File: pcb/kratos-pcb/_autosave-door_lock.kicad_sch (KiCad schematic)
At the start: 8 parts, among them IC1 SN74HC595N, Q2 2N2222A, Q3 2N2222A, U2 74HC595

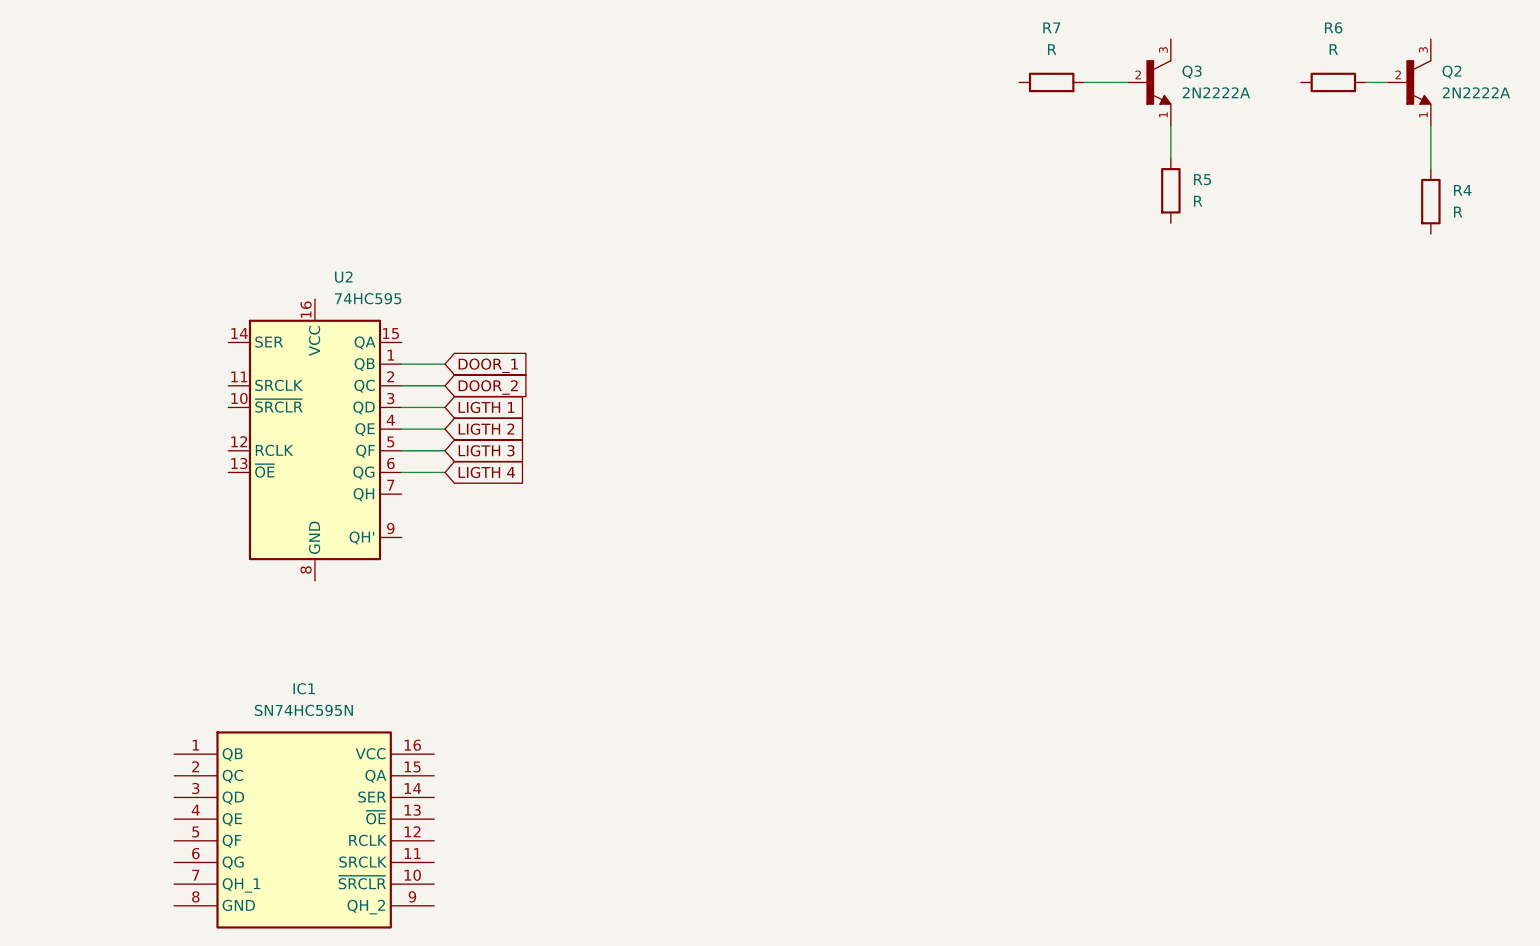
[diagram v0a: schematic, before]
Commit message: ### added  - kicad components
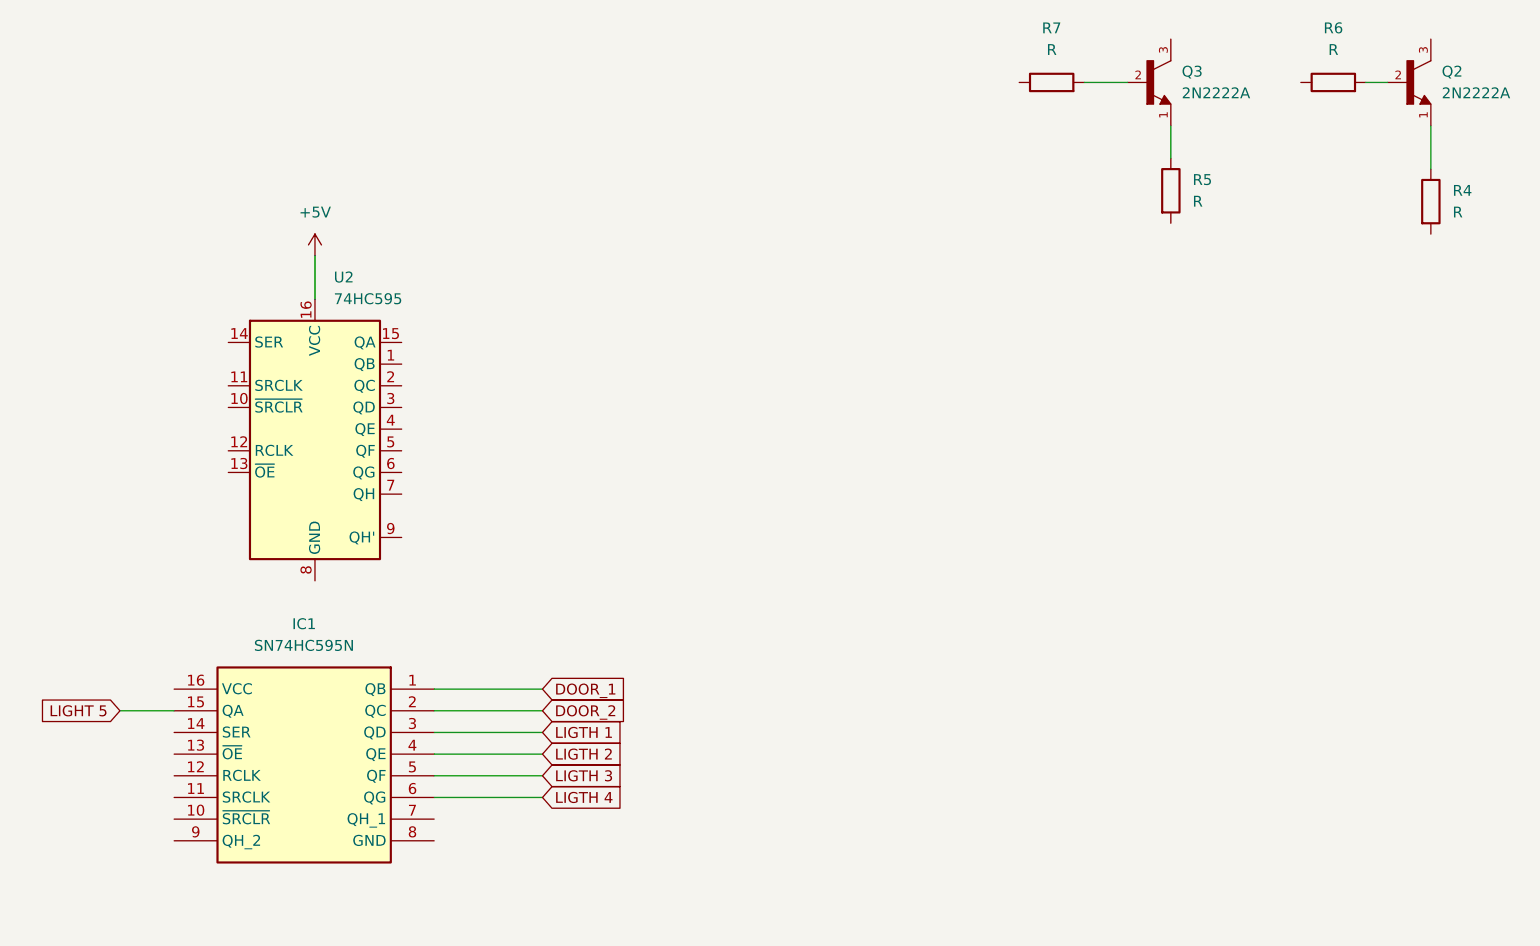
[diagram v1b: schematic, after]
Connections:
- net DOOR_1: now also IC1.1 (QB); no longer U2.1 (QB)
- net DOOR_2: now also IC1.2 (QC); no longer U2.2 (QC)
- net LIGTH 1: now also IC1.3 (QD); no longer U2.3 (QD)
- net LIGTH 2: now also IC1.4 (QE); no longer U2.4 (QE)
- net LIGTH 3: now also IC1.5 (QF); no longer U2.5 (QF)
- net LIGTH 4: now also IC1.6 (QG); no longer U2.6 (QG)
- net LIGHT 5: now reaches IC1.15 (QA)
- net +5V: now reaches U2.16 (VCC)
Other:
- moved on the sheet: IC1
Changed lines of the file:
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@@
     (stroke (width 0) (type default))
   )
-  (wire (pts (xy 124.46 81.28) (xy 129.54 81.28))
+  (wire (pts (xy 128.27 121.92) (xy 140.97 121.92))
+    (stroke (width 0) (type default))
+  )
+  (wire (pts (xy 114.3 58.42) (xy 114.3 63.5))
+    (stroke (width 0) (type default))
+  )
+  (wire (pts (xy 128.27 119.38) (xy 140.97 119.38))
     (stroke (width 0) (type default))
   )
@@
     (stroke (width 0) (type default))
   )
-  (wire (pts (xy 124.46 78.74) (xy 129.54 78.74))
-    (stroke (width 0) (type default))
-  )
-  (wire (pts (xy 124.46 83.82) (xy 129.54 83.82))
-    (stroke (width 0) (type default))
-  )
-  (wire (pts (xy 124.46 71.12) (xy 129.54 71.12))
-    (stroke (width 0) (type default))
-  )
-  (wire (pts (xy 124.46 76.2) (xy 129.54 76.2))
-    (stroke (width 0) (type default))
-  )
-  (wire (pts (xy 124.46 73.66) (xy 129.54 73.66))
+  (wire (pts (xy 128.27 111.76) (xy 140.97 111.76))
+    (stroke (width 0) (type default))
+  )
+  (wire (pts (xy 128.27 116.84) (xy 140.97 116.84))
+    (stroke (width 0) (type default))
+  )
+  (wire (pts (xy 91.44 111.76) (xy 97.79 111.76))
+    (stroke (width 0) (type default))
+  )
+  (wire (pts (xy 128.27 114.3) (xy 140.97 114.3))
+    (stroke (width 0) (type default))
+  )
+  (wire (pts (xy 128.27 109.22) (xy 140.97 109.22))
     (stroke (width 0) (type default))
   )
@@
     (stroke (width 0) (type default))
   )
-  (global_label "LIGTH 4" (shape input) (at 129.54 83.82 0) (fields_autoplaced)
-    (effects (font (size 1.27 1.27)) (justify left))
-    (property "Intersheetrefs" "${INTERSHEET_REFS}" (at 139.9033 83.82 0)
-      (effects (font (size 1.27 1.27)) (justify left) hide)
-    )
-  )
-  (global_label "DOOR_1" (shape input) (at 129.54 71.12 0) (fields_autoplaced)
-    (effects (font (size 1.27 1.27)) (justify left))
-    (property "Intersheetrefs" "${INTERSHEET_REFS}" (at 139.9033 71.12 0)
-      (effects (font (size 1.27 1.27)) (justify left) hide)
-    )
-  )
-  (global_label "LIGTH 3" (shape input) (at 129.54 81.28 0) (fields_autoplaced)
-    (effects (font (size 1.27 1.27)) (justify left))
-    (property "Intersheetrefs" "${INTERSHEET_REFS}" (at 139.9033 81.28 0)
-      (effects (font (size 1.27 1.27)) (justify left) hide)
-    )
-  )
-  (global_label "LIGTH 1" (shape input) (at 129.54 76.2 0) (fields_autoplaced)
-    (effects (font (size 1.27 1.27)) (justify left))
-    (property "Intersheetrefs" "${INTERSHEET_REFS}" (at 139.9033 76.2 0)
-      (effects (font (size 1.27 1.27)) (justify left) hide)
-    )
-  )
-  (global_label "DOOR_2" (shape input) (at 129.54 73.66 0) (fields_autoplaced)
-    (effects (font (size 1.27 1.27)) (justify left))
-    (property "Intersheetrefs" "${INTERSHEET_REFS}" (at 139.9033 73.66 0)
-      (effects (font (size 1.27 1.27)) (justify left) hide)
-    )
-  )
-  (global_label "LIGTH 2" (shape input) (at 129.54 78.74 0) (fields_autoplaced)
-    (effects (font (size 1.27 1.27)) (justify left))
-    (property "Intersheetrefs" "${INTERSHEET_REFS}" (at 139.9033 78.74 0)
+  (global_label "LIGTH 4" (shape input) (at 140.97 121.92 0) (fields_autoplaced)
+    (effects (font (size 1.27 1.27)) (justify left))
+    (property "Intersheetrefs" "${INTERSHEET_REFS}" (at 151.3333 121.92 0)
+      (effects (font (size 1.27 1.27)) (justify left) hide)
+    )
+  )
+  (global_label "LIGTH 3" (shape input) (at 140.97 119.38 0) (fields_autoplaced)
+    (effects (font (size 1.27 1.27)) (justify left))
+    (property "Intersheetrefs" "${INTERSHEET_REFS}" (at 151.3333 119.38 0)
+      (effects (font (size 1.27 1.27)) (justify left) hide)
+    )
+  )
+  (global_label "DOOR_2" (shape input) (at 140.97 111.76 0) (fields_autoplaced)
+    (effects (font (size 1.27 1.27)) (justify left))
+    (property "Intersheetrefs" "${INTERSHEET_REFS}" (at 151.3333 111.76 0)
+      (effects (font (size 1.27 1.27)) (justify left) hide)
+    )
+  )
+  (global_label "LIGTH 2" (shape input) (at 140.97 116.84 0) (fields_autoplaced)
+    (effects (font (size 1.27 1.27)) (justify left))
+    (property "Intersheetrefs" "${INTERSHEET_REFS}" (at 151.3333 116.84 0)
+      (effects (font (size 1.27 1.27)) (justify left) hide)
+    )
+  )
+  (global_label "LIGHT 5" (shape input) (at 91.44 111.76 180) (fields_autoplaced)
+    (effects (font (size 1.27 1.27)) (justify right))
+    (property "Intersheetrefs" "${INTERSHEET_REFS}" (at 81.0767 111.76 0)
+      (effects (font (size 1.27 1.27)) (justify right) hide)
+    )
+  )
+  (global_label "LIGTH 1" (shape input) (at 140.97 114.3 0) (fields_autoplaced)
+    (effects (font (size 1.27 1.27)) (justify left))
+    (property "Intersheetrefs" "${INTERSHEET_REFS}" (at 151.3333 114.3 0)
+      (effects (font (size 1.27 1.27)) (justify left) hide)
+    )
+  )
+  (global_label "DOOR_1" (shape input) (at 140.97 109.22 0) (fields_autoplaced)
+    (effects (font (size 1.27 1.27)) (justify left))
+    (property "Intersheetrefs" "${INTERSHEET_REFS}" (at 151.3333 109.22 0)
       (effects (font (size 1.27 1.27)) (justify left) hide)
     )
@@
     )
   )
-  (symbol (lib_id "SN74HC595N:SN74HC595N") (at 97.79 116.84 0) (unit 1)
-    (in_bom yes) (on_board yes) (dnp no) (fields_autoplaced)
-    (property "Reference" "IC1" (at 113.03 109.22 0)
-      (effects (font (size 1.27 1.27)))
-    )
-    (property "Value" "SN74HC595N" (at 113.03 111.76 0)
-      (effects (font (size 1.27 1.27)))
-    )
-    (property "Footprint" "DIP794W53P254L1930H508Q16N" (at 124.46 211.76 0)
-      (effects (font (size 1.27 1.27)) (justify left top) hide)
-    )
-    (property "Datasheet" "http://www.ti.com/lit/ds/symlink/sn74hc595.pdf" (at 124.46 311.76 0)
-      (effects (font (size 1.27 1.27)) (justify left top) hide)
-    )
-    (property "Height" "5.08" (at 124.46 511.76 0)
-      (effects (font (size 1.27 1.27)) (justify left top) hide)
-    )
-    (property "Mouser Part Number" "595-SN74HC595N" (at 124.46 611.76 0)
-      (effects (font (size 1.27 1.27)) (justify left top) hide)
-    )
-    (property "Mouser Price/Stock" "https://www.mouser.co.uk/ProductDetail/Texas-Instruments/SN74HC595N?qs=IEl3ej0IqwBTHkYa8XPoMQ%3D%3D" (at 124.46 711.76 0)
-      (effects (font (size 1.27 1.27)) (justify left top) hide)
-    )
-    (property "Manufacturer_Name" "Texas Instruments" (at 124.46 811.76 0)
-      (effects (font (size 1.27 1.27)) (justify left top) hide)
-    )
-    (property "Manufacturer_Part_Number" "SN74HC595N" (at 124.46 911.76 0)
+  (symbol (lib_id "SN74HC595N:SN74HC595N") (at 128.27 109.22 0) (mirror y) (unit 1)
+    (in_bom yes) (on_board yes) (dnp no)
+    (property "Reference" "IC1" (at 113.03 101.6 0)
+      (effects (font (size 1.27 1.27)))
+    )
+    (property "Value" "SN74HC595N" (at 113.03 104.14 0)
+      (effects (font (size 1.27 1.27)))
+    )
+    (property "Footprint" "DIP794W53P254L1930H508Q16N" (at 101.6 204.14 0)
+      (effects (font (size 1.27 1.27)) (justify left top) hide)
+    )
+    (property "Datasheet" "http://www.ti.com/lit/ds/symlink/sn74hc595.pdf" (at 101.6 304.14 0)
+      (effects (font (size 1.27 1.27)) (justify left top) hide)
+    )
+    (property "Height" "5.08" (at 101.6 504.14 0)
+      (effects (font (size 1.27 1.27)) (justify left top) hide)
+    )
+    (property "Mouser Part Number" "595-SN74HC595N" (at 101.6 604.14 0)
+      (effects (font (size 1.27 1.27)) (justify left top) hide)
+    )
+    (property "Mouser Price/Stock" "https://www.mouser.co.uk/ProductDetail/Texas-Instruments/SN74HC595N?qs=IEl3ej0IqwBTHkYa8XPoMQ%3D%3D" (at 101.6 704.14 0)
+      (effects (font (size 1.27 1.27)) (justify left top) hide)
+    )
+    (property "Manufacturer_Name" "Texas Instruments" (at 101.6 804.14 0)
+      (effects (font (size 1.27 1.27)) (justify left top) hide)
+    )
+    (property "Manufacturer_Part_Number" "SN74HC595N" (at 101.6 904.14 0)
       (effects (font (size 1.27 1.27)) (justify left top) hide)
     )
@@
         )
       )
+    )
+  )
+  (symbol (lib_id "power:+5V") (at 114.3 58.42 0) (unit 1)
+    (in_bom yes) (on_board yes) (dnp no) (fields_autoplaced)
+    (property "Reference" "#PWR010" (at 114.3 62.23 0)
+      (effects (font (size 1.27 1.27)) hide)
+    )
+    (property "Value" "+5V" (at 114.3 53.34 0)
+      (effects (font (size 1.27 1.27)))
+    )
+    (property "Footprint" "" (at 114.3 58.42 0)
+      (effects (font (size 1.27 1.27)) hide)
+    )
+    (property "Datasheet" "" (at 114.3 58.42 0)
+      (effects (font (size 1.27 1.27)) hide)
+    )
+    (pin "1")
+    (instances
+      (project "kratos-pcb"
+        (path "/12f1b997-8c5f-4ef7-b036-7873ddaba48e/bcabd817-9513-4d0c-a70f-0efd675264f1"
+          (reference "#PWR010") (unit 1)
+        )
+      )

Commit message: ### Added
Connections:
- net DOOR_1: now also U2.1 (QB); no longer IC1.1 (QB)
- net DOOR_2: now also U2.2 (QC); no longer IC1.2 (QC)
- net LIGTH 1: now also U2.3 (QD); no longer IC1.3 (QD)
- net LIGTH 2: now also U2.4 (QE); no longer IC1.4 (QE)
- net LIGTH 3: now also U2.5 (QF); no longer IC1.5 (QF)
- net LIGTH 4: now also U2.6 (QG); no longer IC1.6 (QG)
- net +5V: no longer names the net of U2.16 (VCC)
- net LIGHT 5: no longer names the net of IC1.15 (QA)
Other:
- moved on the sheet: IC1, Q2, Q3, R4, R5, R6, R7
